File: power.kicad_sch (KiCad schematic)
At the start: 21 parts, among them J101 BATT pads, Q101 DMG3401LSN-7, SW101 PWR, U101 TPS63001

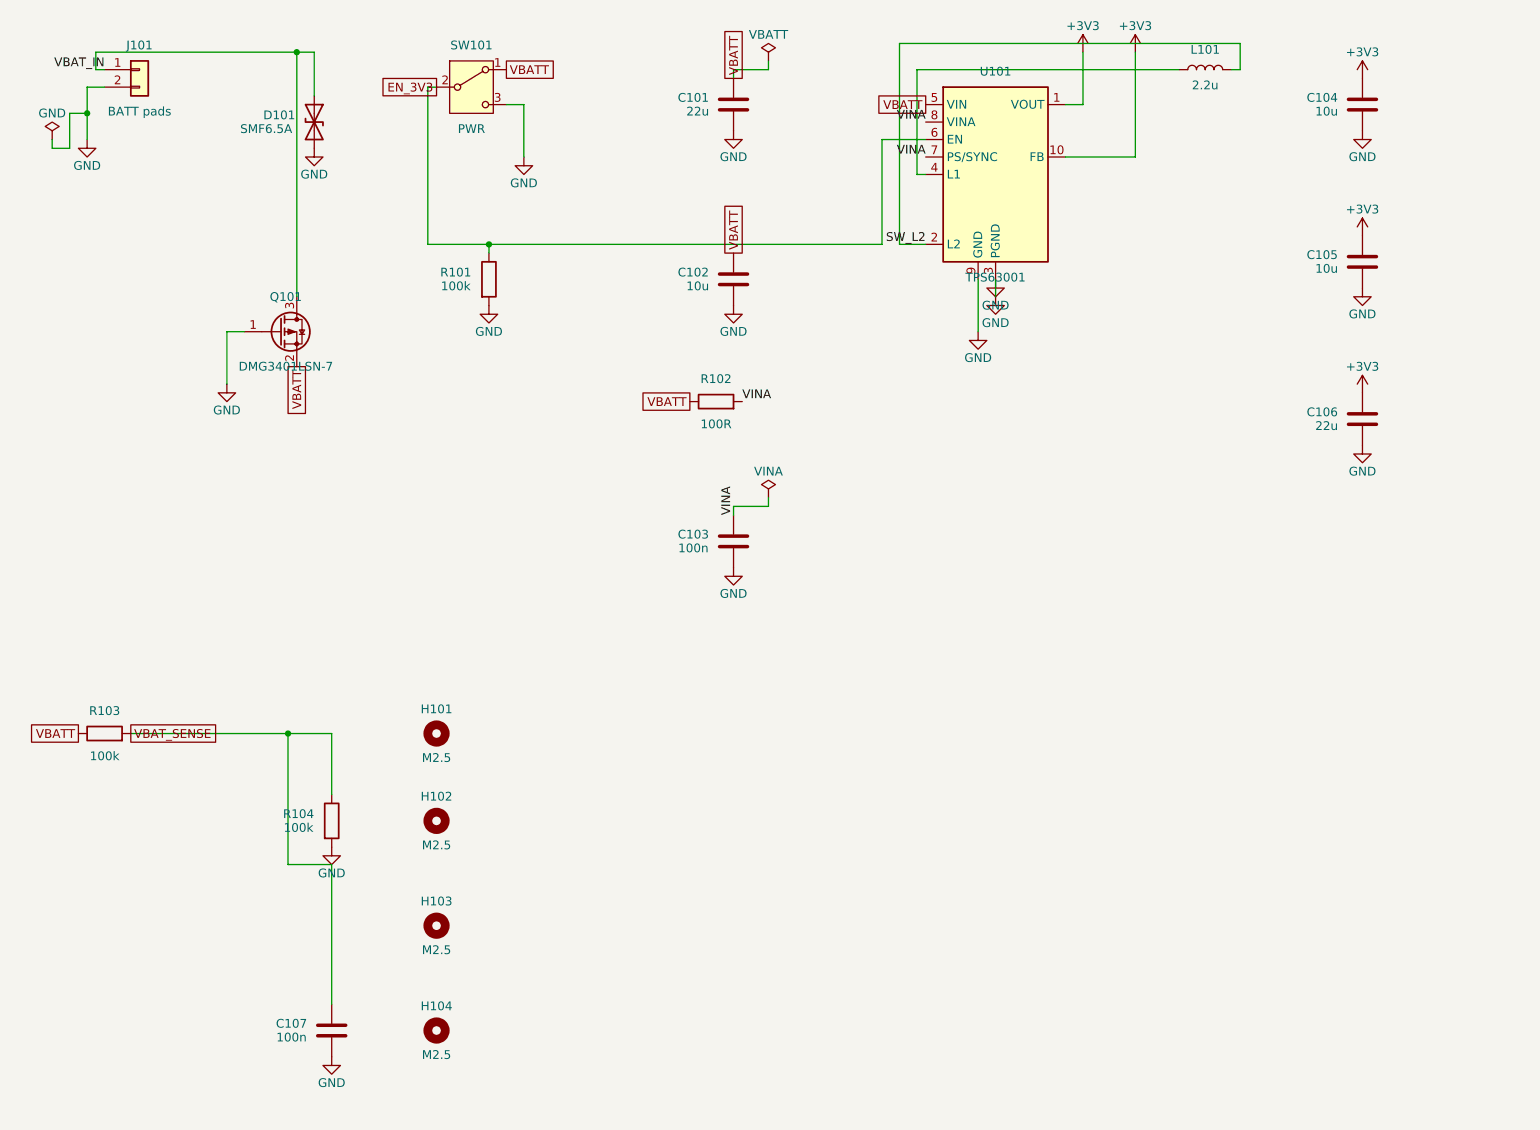
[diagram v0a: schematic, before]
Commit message: Remove the buck-boost: run straight off a 3.6 V max cell
The TPS63001 and its inductor come out and the battery drives the board
directly, so the rail is renamed +3V3 -> +BATT on every sheet: a net called
3V3 that is really the cell is the kind of label someone connects a charger
to.

SW101 used to switch the converter's EN pin, which is why it was never in
series with the load - the C&K JS series is rated 300 mA and this board
peaks past that. With no EN pin it now drives the gate of Q102, a second
DMG3401LSN-7 back to back with the reverse-block Q101. Q101 keeps its source
on the load side so its body diode conducts forward, which is exactly why it
cannot also be the switch; Q102 faces the other way so an open channel
really disconnects.

R102/C102 are re-used as a 10k/1u gate network giving about 9 ms of soft
start, replacing the converter's. Without it the switch would connect ~70 uF
of rail and IC decoupling straight across a cell that may have ohms of
internal resistance. The 10k stays small against the 100k pull-up so the
gate still reaches 91 % of VBATT.

The R103/R104 sense divider moves from VBATT to the switched +BATT, so it
draws nothing with the board off.

Also fixes assemble.ts rewriting cc1200_balloon.kicad_pro from a fixed
template every build, which was silently resetting the net classes, board
design settings and ERC severities KiCad had written. Found while rebuilding
for this change.

Gates: placement 5/5, routing DRC 0, netlist matches sheets/*.json at 378
endpoints / 76 nets, full-hierarchy ERC 0 errors and the 2 known BME688
address-strap warnings. Build output is byte-identical across runs.

The large .kicad_sch diffs are formatting: the committed set had been opened
and saved by KiCad, which expands the compact s-expressions the generator
writes. Nothing but the power sheet and the rail name changed electrically.

Not done: cc1200_balloon.kicad_pcb still carries U101, L101 and C105 and has
no Q102. It needs Update PCB from Schematic.

Co-Au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
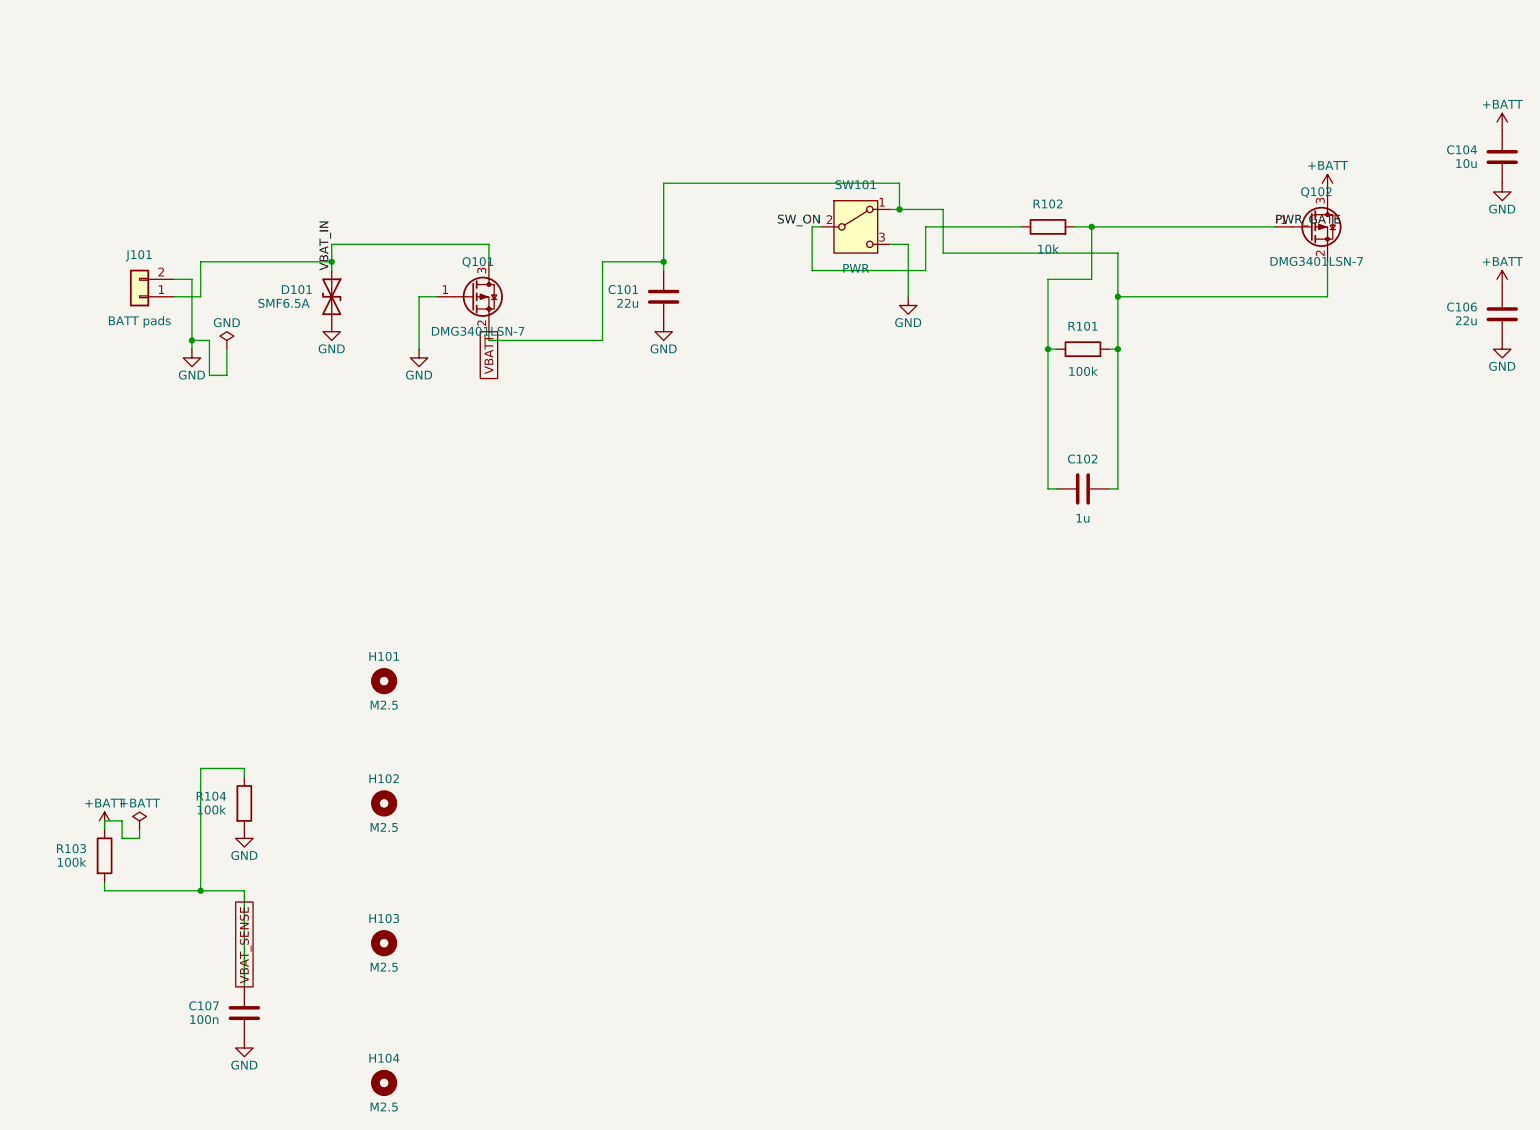
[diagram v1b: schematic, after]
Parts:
- removed C103: 100n, Capacitor_SMD:C_0402_1005Metric, symbol Device:C
- removed C105: 10u, Capacitor_SMD:C_0603_1608Metric, symbol Device:C
- removed L101: 2.2u, Inductor_SMD:L_1008_2520Metric, symbol Device:L
- removed U101: TPS63001, Package_SON:VSON-10-1EP_3x3mm_P0.5mm_EP1.65x2.4mm, symbol Regulator_Switching:TPS63001
- added Q102: DMG3401LSN-7, Package_TO_SOT_SMD:SOT-23, symbol Transistor_FET:Q_PMOS_GSD
- C102: value 10u -> 1u; footprint Capacitor_SMD:C_0603_1608Metric -> Capacitor_SMD:C_0402_1005Metric
- R102: value 100R -> 10k
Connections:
- net VINA is gone; now on net PWR_GATE: R102.2
- net GND: no longer C102.2, R101.2
- net VBATT: now also C102.2, R101.2, Q102.2 (S); no longer C102.1, R102.1, R103.1
- net +3V3 renamed +BATT
- net +BATT: now also R103.1, Q102.3 (D)
- net EN_3V3 renamed PWR_GATE
- net PWR_GATE: now also C102.1, Q102.1 (G); no longer SW101.2 (B)
- new net SW_ON: R102.1, SW101.2 (B)
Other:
- title: Power: battery input, reverse protection, 3V3 buck-boost -> Power: battery input, reverse protection, P-FET load switch
- moved on the sheet: C101, C102, C104, C106, C107, D101, H101, H102, H103, H104, J101, Q101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
